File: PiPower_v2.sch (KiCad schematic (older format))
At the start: 82 parts, among them J1 MicroUSB_in, J10 5V_Pi, J11 12V_Out, J2 LiPo_JST, J3 USB_A_out, J4 Auto_On, J5 5V_USB, J6 5V_EXT, J7 5V_IN, J8 VBAT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

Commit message: 1310211033 PiPower work in progress
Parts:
- removed Q1: 2SK3019, SOT416_2SK3019, symbol 2SK3019
- removed R5: 100k, r_0805, symbol R
- removed R7: 10k, r_0805, symbol R
- R9: value 1k5 -> 4k7
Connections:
- net labels removed: EN
- wire segments 352 -> 242

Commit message: 1310271049 PiPower work in progress
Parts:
- added L?: 4u7H,1.2A, Inductor_SMD1, symbol INDUCTOR
- added R?: 100k, r_0805, symbol R
- added U2: TPS62163, symbol TPS62163
- C2: value 100u,25V -> 10u,25V, X7R
- C3: value 2u2 Tant -> 22u,25V, X7R
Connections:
- wire segments 242 -> 254
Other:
- moved on the sheet: C1, C2, C3, D1, J6
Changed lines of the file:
@@
 Text Label 7875 1050 0    40   ~ 0
 PWR_IN
-$Comp
-L GND #PWR1
-U 1 1 51E42797
-P 9700 1800
-F 0 "#PWR1" H 9700 1800 30  0001 C CNN
-F 1 "GND" H 9700 1730 30  0001 C CNN
-F 2 "" H 9700 1800 60  0001 C CNN
-F 3 "" H 9700 1800 60  0001 C CNN
-	1    9700 1800
-	-1   0    0    -1
-$EndComp
-Text Label 8900 1700 0    40   ~ 0
+Text Label 9600 1650 0    40   ~ 0
 GND
 $Comp
@@
 L DIODESCH D1
 U 1 1 51E427BE
-P 8300 1050
-F 0 "D1" H 8300 1150 40  0000 C CNN
-F 1 "LSM115J" H 8300 950 40  0000 C CNN
-F 2 "diode-DO214BA" H 8300 1050 60  0001 C CNN
-F 3 "~" H 8300 1050 60  0000 C CNN
-	1    8300 1050
-	1    0    0    -1
-$EndComp
-Text Label 9975 1050 0    40   ~ 0
+P 11700 450
+F 0 "D1" H 11700 550 40  0000 C CNN
+F 1 "LSM115J" H 11700 350 40  0000 C CNN
+F 2 "diode-DO214BA" H 11700 450 60  0001 C CNN
+F 3 "~" H 11700 450 60  0000 C CNN
+	1    11700 450
+	1    0    0    -1
+$EndComp
+Text Label 10100 1050 0    40   ~ 0
 5V_EXT
 $Comp
 L CAP_NP C1
 U 1 1 51E43023
-P 9700 1475
-F 0 "C1" H 9625 1400 40  0000 C CNN
-F 1 "100nF" H 9600 1575 40  0000 C CNN
-F 2 "c_0805" H 9700 1475 60  0001 C CNN
-F 3 "" H 9700 1475 60  0000 C CNN
-	1    9700 1475
+P 10325 1175
+F 0 "C1" H 10250 1100 40  0000 C CNN
+F 1 "100nF" V 10275 1350 40  0000 C CNN
+F 2 "c_0805" H 10325 1175 60  0001 C CNN
+F 3 "" H 10325 1175 60  0000 C CNN
+	1    10325 1175
 	-1   0    0    1
 $EndComp
@@
 L CAP_POL C2
 U 1 1 51E43043
-P 8575 1500
-F 0 "C2" H 8650 1600 40  0000 C CNN
-F 1 "100u,25V" H 8725 1425 40  0000 C CNN
-F 2 "C_ELCO_SMD" H 8575 1500 60  0001 C CNN
-F 3 "" H 8575 1500 60  0000 C CNN
-	1    8575 1500
+P 8175 1200
+F 0 "C2" H 8225 1275 40  0000 C CNN
+F 1 "10u,25V, X7R" V 8225 950 40  0000 C CNN
+F 2 "C_ELCO_SMD" H 8175 1200 60  0001 C CNN
+F 3 "" H 8175 1200 60  0000 C CNN
+	1    8175 1200
 	1    0    0    -1
 $EndComp
@@
 L CAP_POL C3
 U 1 1 51E4306C
-P 9975 1500
-F 0 "C3" H 10050 1600 40  0000 C CNN
-F 1 "2u2 Tant" H 10125 1425 40  0000 C CNN
-F 2 "c_0805" H 9975 1500 60  0001 C CNN
-F 3 "" H 9975 1500 60  0000 C CNN
-	1    9975 1500
+P 10075 1200
+F 0 "C3" H 10150 1300 40  0000 C CNN
+F 1 "22u,25V, X7R" V 10125 950 40  0000 C CNN
+F 2 "c_0805" H 10075 1200 60  0001 C CNN
+F 3 "" H 10075 1200 60  0000 C CNN
+	1    10075 1200
 	1    0    0    -1
 $EndComp
@@
 L CONN_2 J6
 U 1 1 51EBDA2C
-P 10675 1400
-F 0 "J6" V 10625 1400 40  0000 C CNN
-F 1 "5V_EXT" V 10725 1400 40  0000 C CNN
-F 2 "Header_2" H 10675 1300 60  0001 C CNN
-F 3 "~" H 10675 1300 60  0000 C CNN
-	1    10675 1400
+P 10900 1150
+F 0 "J6" V 10850 1150 40  0000 C CNN
+F 1 "5V_EXT" V 10950 1150 40  0000 C CNN
+F 2 "Header_2" H 10900 1050 60  0001 C CNN
+F 3 "~" H 10900 1050 60  0000 C CNN
+	1    10900 1150
 	1    0    0    -1
 $EndComp
@@
 L NCP1117ST50 U2
 U 1 1 52161420
-P 9150 1200
-F 0 "U2" H 8975 1575 40  0000 C CNN
-F 1 "NCP1117ST50" H 9150 1500 40  0000 C CNN
-F 2 "SOT223" H 9150 1200 60  0001 C CNN
-F 3 "~" H 9150 1200 60  0000 C CNN
-	1    9150 1200
+P 11900 1050
+F 0 "U2" H 11725 1425 40  0000 C CNN
+F 1 "NCP1117ST50" H 11900 1350 40  0000 C CNN
+F 2 "SOT223" H 11900 1050 60  0001 C CNN
+F 3 "~" H 11900 1050 60  0000 C CNN
+	1    11900 1050
 	1    0    0    -1
 $EndComp
@@
 Wire Wire Line
 	10125 2850 10125 2975
-Connection ~ 9975 1700
-Wire Wire Line
-	10275 1700 10275 1500
-Wire Wire Line
-	10275 1500 10325 1500
-Connection ~ 9975 1050
-Wire Wire Line
-	10275 1050 10275 1300
-Wire Wire Line
-	10275 1300 10325 1300
 Connection ~ 5400 3375
 Wire Wire Line
@@
 	5550 2125 5550 1900
 Wire Wire Line
-	9550 1050 10275 1050
-Wire Wire Line
-	8575 1050 8575 1400
-Connection ~ 8575 1050
-Wire Wire Line
-	9700 1575 9700 1800
-Wire Wire Line
 	7850 1250 7925 1250
 Wire Wire Line
 	7925 1150 7850 1150
-Connection ~ 9700 1700
-Wire Wire Line
-	9975 1700 9975 1575
-Wire Wire Line
-	9975 1050 9975 1400
-Wire Wire Line
-	8575 1700 10275 1700
-Wire Wire Line
-	8575 1575 8575 1700
-Wire Wire Line
-	7850 1050 8100 1050
+Wire Wire Line
+	7850 1050 8450 1050
 Wire Wire Line
 	7925 1150 7925 1800
-Wire Wire Line
-	9150 1800 9150 1600
-Connection ~ 9150 1700
-Connection ~ 9700 1050
-Wire Wire Line
-	8500 1050 8750 1050
-Wire Wire Line
-	9700 1050 9700 1400
 Wire Wire Line
 	5200 7175 5200 6400
@@
 Wire Wire Line
 	8025 1050 8025 1700
-Connection ~ 8025 1050
 Wire Wire Line
 	7800 1600 7925 1600
 Connection ~ 7925 1600
 Wire Wire Line
-	7800 1800 9150 1800
-Wire Wire Line
 	8025 1700 7800 1700
 Connection ~ 8025 1500
-Connection ~ 7925 1800
 Wire Wire Line
 	1225 1500 1300 1500
@@
 	3250 3375 3100 3375
 Connection ~ 3100 3375
+$Comp
+L TPS62163 U2
+U 1 1 526D1432
+P 8800 1400
+F 0 "U2" H 8550 1850 40  0000 L BNN
+F 1 "TPS62163" H 8550 1050 40  0000 L TNN
+F 2 "" H 8800 1700 60  0000 C CNN
+F 3 "" H 8800 1700 60  0000 C CNN
+	1    8800 1400
+	1    0    0    -1
+$EndComp
+$Comp
+L INDUCTOR L?
+U 1 1 526D14F0
+P 9550 1050
+F 0 "L?" V 9500 1050 40  0000 C CNN
+F 1 "4u7H,1.2A" V 9650 1050 40  0000 C CNN
+F 2 "Inductor_SMD1" H 9550 1050 60  0001 C CNN
+F 3 "~" H 9550 1050 60  0000 C CNN
+	1    9550 1050
+	0    -1   -1   0
+$EndComp
+$Comp
+L R R?
+U 1 1 526D1586
+P 9500 1250
+F 0 "R?" V 9550 1450 40  0000 C CNN
+F 1 "100k" V 9500 1250 40  0000 C CNN
+F 2 "r_0805" H 9500 1250 60  0001 C CNN
+F 3 "" H 9500 1250 60  0000 C CNN
+	1    9500 1250
+	0    -1   -1   0
+$EndComp
+$Comp
+L GND #PWR1
+U 1 1 51E42797
+P 8375 1925
+F 0 "#PWR1" H 8375 1925 30  0001 C CNN
+F 1 "GND" H 8375 1855 30  0001 C CNN
+F 2 "" H 8375 1925 60  0001 C CNN
+F 3 "" H 8375 1925 60  0001 C CNN
+	1    8375 1925
+	-1   0    0    -1
+$EndComp
+Wire Wire Line
+	9150 1150 9925 1150
+Wire Wire Line
+	9925 1050 9925 1250
+Wire Wire Line
+	9850 1050 10550 1050
+Wire Wire Line
+	9250 1050 9150 1050
+Wire Wire Line
+	10075 1050 10075 1100
+Wire Wire Line
+	10325 1050 10325 1100
+Wire Wire Line
+	9150 1250 9250 1250
+Wire Wire Line
+	9925 1250 9750 1250
+Connection ~ 9925 1150
+Connection ~ 10075 1050
+Connection ~ 9925 1050
+Wire Wire Line
+	10325 1275 10325 1650
+Wire Wire Line
+	9150 1650 10475 1650
+Wire Wire Line
+	9150 1350 9250 1350
+Wire Wire Line
+	9250 1350 9250 1800
+Connection ~ 9250 1650
+Wire Wire Line
+	9150 1550 9250 1550
+Connection ~ 9250 1550
+Wire Wire Line
+	8175 1050 8175 1100
+Wire Wire Line
+	8450 1150 8375 1150
+Wire Wire Line
+	8375 1150 8375 1050
+Connection ~ 8375 1050
+Wire Wire Line
+	8450 1250 8375 1250
+Wire Wire Line
+	8175 1650 8450 1650
+Wire Wire Line
+	8375 1250 8375 1925
+Wire Wire Line
+	8450 1350 8375 1350
+Connection ~ 8375 1350
+Wire Wire Line
+	8450 1450 8375 1450
+Connection ~ 8375 1450
+Wire Wire Line
+	8450 1550 8375 1550
+Connection ~ 8375 1550
+Wire Wire Line
+	8175 1275 8175 1650
+Connection ~ 8375 1650
+Connection ~ 10325 1050
+Wire Wire Line
+	10550 1250 10475 1250
+Wire Wire Line
+	10475 1250 10475 1650
+Connection ~ 10325 1650
+Wire Wire Line
+	10075 1275 10075 1650
+Connection ~ 10075 1650
+Connection ~ 8175 1050
+Connection ~ 8025 1050
+Connection ~ 7925 1800
+Wire Wire Line
+	9250 1800 7800 1800
+Connection ~ 8375 1800
 $EndSCHEMATC

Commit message: 1311021119 Schematic complete, needs to be verified
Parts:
- removed D1, D5: LSM115J, diode-DO214BA, symbol DIODESCH
- removed SJ5: STAT, ShortLink, symbol LINK1
- removed U2: NCP1117ST50, SOT223, symbol NCP1117ST50
- added J12: 5V_IN, symbol CONN_3
- added SJ5: STAT, symbol LINK2
- D7: value EXT_ON -> 5V_OUT
- J7: value 5V_IN -> 5V_OUT
- SJ2: value Ext_On -> 5V_OUT
- gave numbers to parts that had none: 2
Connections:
- net labels added: 5V_OUT
- wire segments 254 -> 256
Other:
- note added: "12V INPUT (5V-12V)"
- note added: "5V USB INPUT"
- note added: "Auto-Switch (5V_IN <> 5V_BAT)"
- note added: "Boost Converter (3.7V to 5V Bat)"
- note added: "LiPo Charger (3.7V)"
- note added: "LiPo Fuel Gauge I2C"
- note added: "Manual Selector"
- note added: "Power Switch"
- note added: "Ras-Pi GPIO Header"
- note removed: "3.7V to 5V Boost Conv.\nVBAT is LiPo 3.7V\n5V_BAT is output from Boost conv\n\nEN input of U4 controls auto-switching.\nWhen 5V_IN is On, EN is LOW, U4 is SHUT\nWhen 5V_IN is Off, EN is HI, U4 OPERATES"
- note removed: "5V INPUT at J2, Micro USB\nU1 charges 3.7V LiPo\nLiPo connects to J3\n\nEDIT :\nR3 changed from \n1k5 (500mA) to 4k7 (200mA)\n\nR1/R2 changed from\n1k5 to 4k7\n\nAdded Shorting Link for LEDs"
- note removed: "Auto Switch selector\nExt 12V <> uUSB 5V\n\nAdded Jumper link\nto disable LED"
- note removed: "Ext 7V to 12V Barrel Socket"
- note removed: "Li-Po Battery\nFuel Gauge"
- note removed: "Power Switcher.\n5V_Pi to Ras-Pi\nGPIO4 monitored on Ras-Pi\nSW1 to switch On/Off Ras-Pi\nJumper J1 allows Auto On. \n ON = Ras-Pi On when power applied\n OFF = Ras-Pi to be turned On by SW1\nR21 prevents Ras-Pi GPIO4 damage due to 5V\n\nNormal operation : 5V_IN from uUSB powers Ras-Pi\nLiPo is charged via U1\n5V_BAT cannot operate Ras-Pi due to D5 reverse bias\nWhen 5V_IN is cut off, 5V_BAT powe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"
- note removed: "Swapped Off and On on J4\nAdded LED for 5V_Pi indication\nAdded 470k (R23)"
- moved on the sheet: C1, C10, C11, C12, C13, C14, C15, C16, C17, C18, C2, C3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

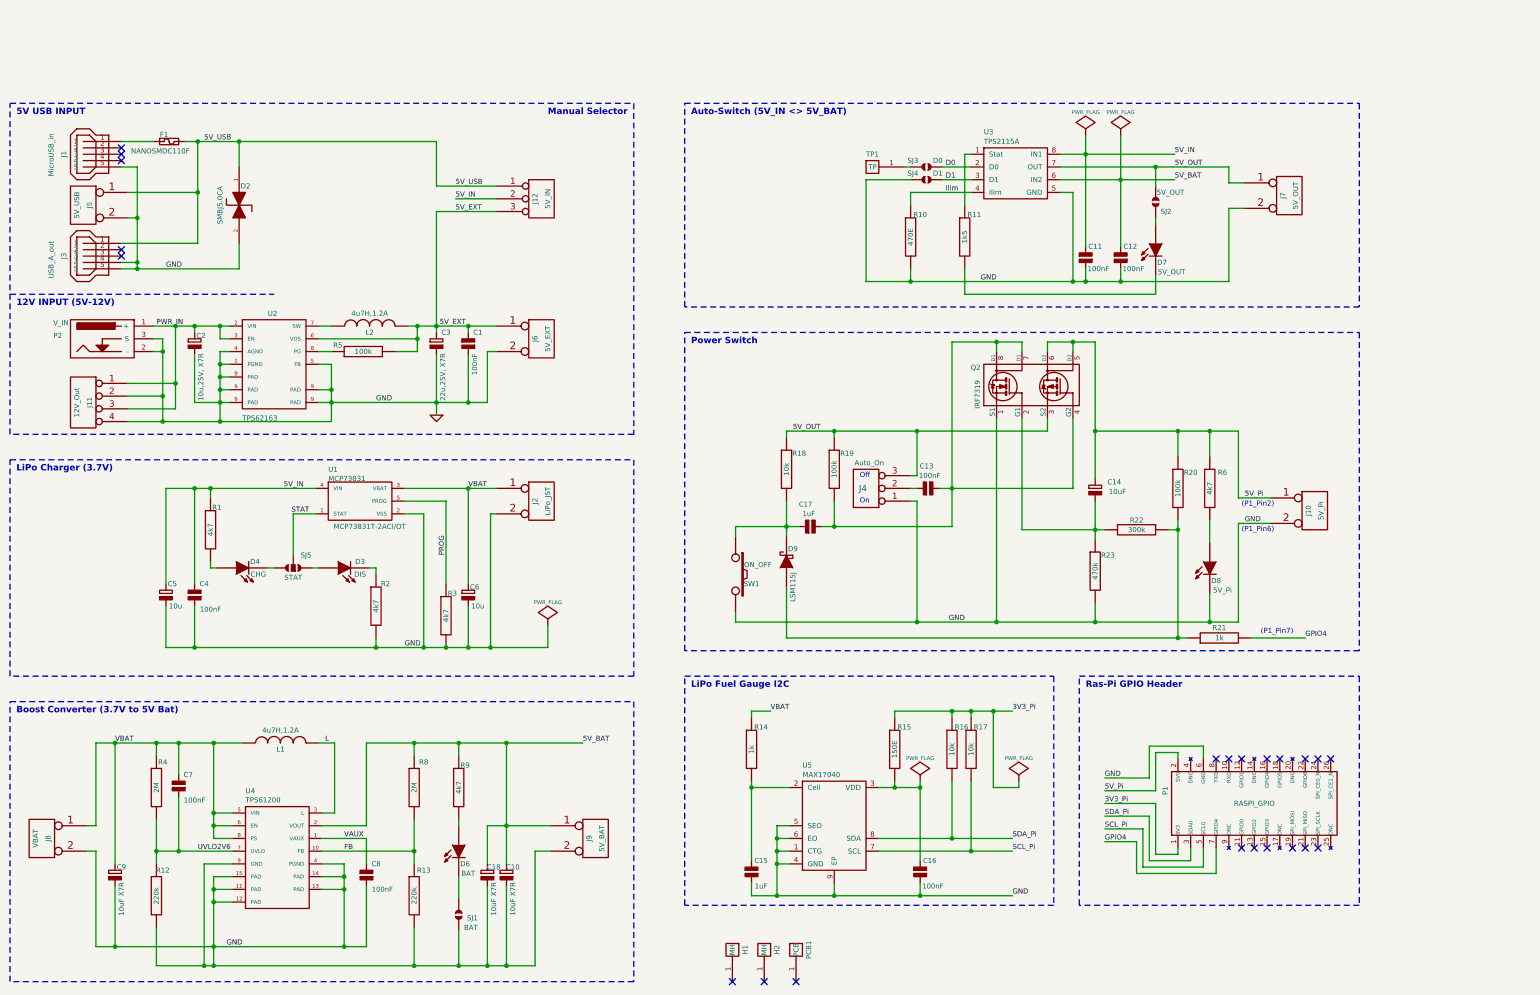
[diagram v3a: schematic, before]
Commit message: 1311031620 Schematic complete, needs to be verified
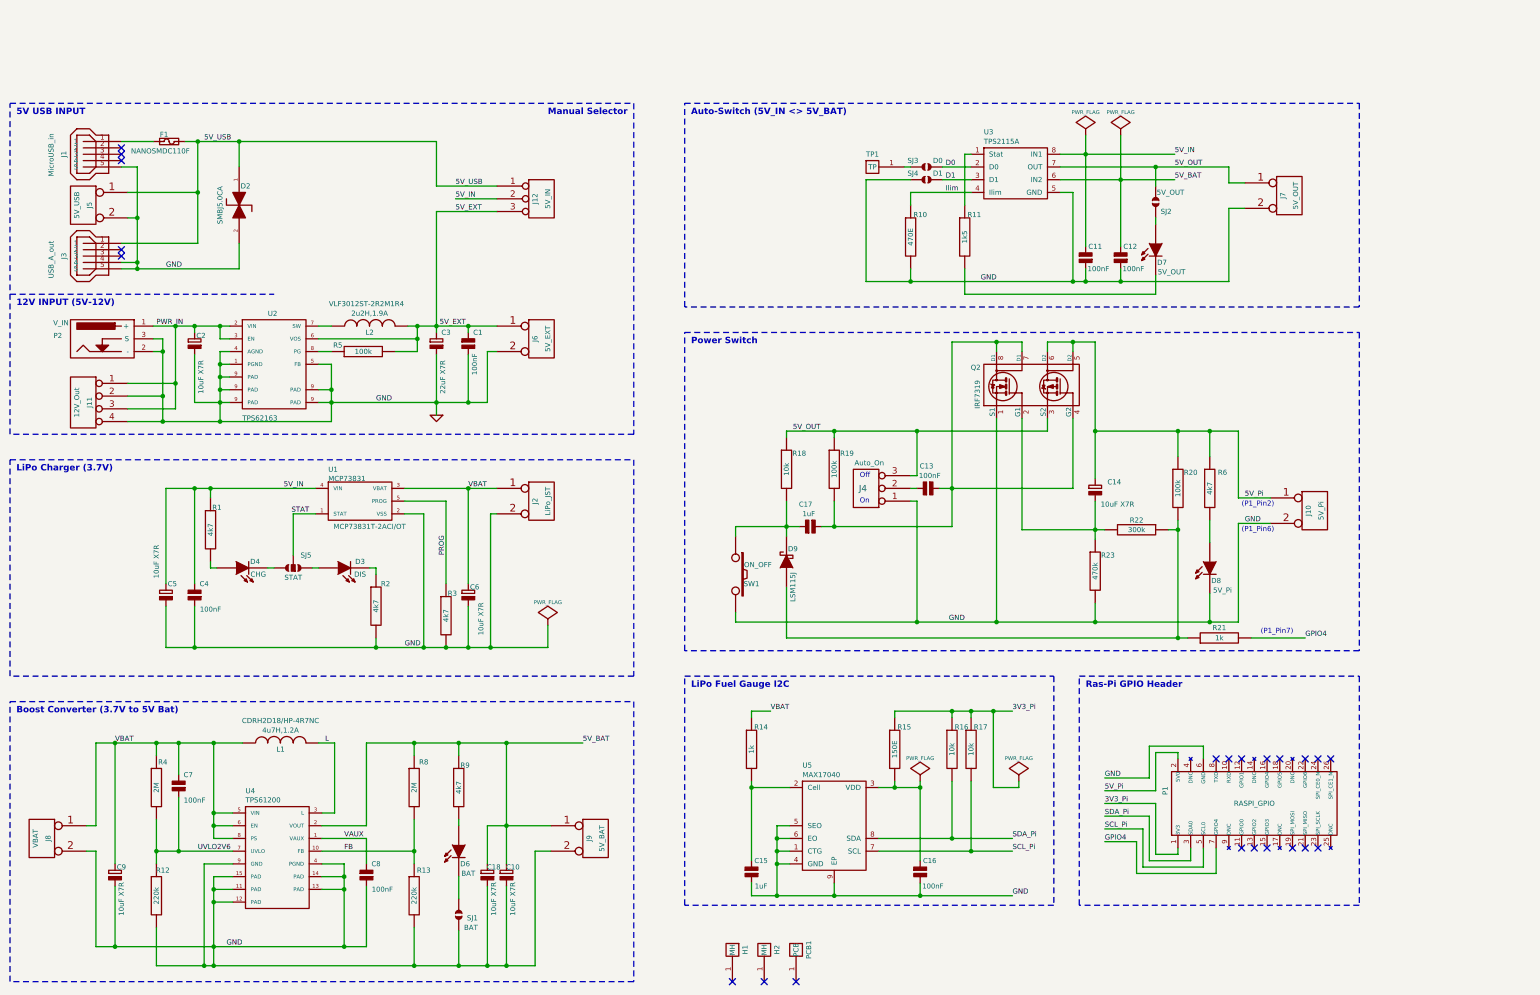
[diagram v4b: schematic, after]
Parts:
- C14: value 10uF -> 10uF X7R
- C2: value 10u,25V, X7R -> 10uF X7R
- C3: value 22u,25V, X7R -> 22uF X7R
- C5, C6: value 10u -> 10uF X7R
- L1: Mfr_PN (none) -> CDRH2D18/HP-4R7NC
- L2: value 4u7H,1.2A -> 2u2H,1.9A; Mfr_PN (none) -> VLF3012ST-2R2M1R4
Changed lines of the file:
@@
 P 9075 3700
 F 0 "C14" H 9225 3775 40  0000 C CNN
-F 1 "10uF" H 9250 3700 40  0000 C CNN
+F 1 "10uF X7R" H 9250 3600 40  0000 C CNN
 F 2 "C_ELCO_SMD" H 9075 3700 60  0001 C CNN
 F 3 "" H 9075 3700 60  0000 C CNN
@@
 P 1775 4525
 F 0 "C5" H 1825 4625 40  0000 C CNN
-F 1 "10u" H 1850 4450 40  0000 C CNN
+F 1 "10uF X7R" V 1700 4800 40  0000 C CNN
 F 2 "C_ELCO_SMD" H 1775 4525 60  0001 C CNN
 F 3 "" H 1775 4525 60  0000 C CNN
@@
 P 4150 4525
 F 0 "C6" H 4200 4600 40  0000 C CNN
-F 1 "10u" H 4225 4450 39  0000 C CNN
+F 1 "10uF X7R" V 4250 4350 39  0000 C CNN
 F 2 "C_ELCO_SMD" H 4150 4525 60  0001 C CNN
 F 3 "" H 4150 4525 60  0000 C CNN
@@
 F 2 "Inductor_SMD1" H 2675 5675 60  0001 C CNN
 F 3 "~" H 2675 5675 60  0000 C CNN
+F 4 "CDRH2D18/HP-4R7NC" V 2850 5675 40  0000 C CNN "Mfr_PN"
 	1    2675 5675
 	0    -1   -1   0
@@
 P 2000 2550
 F 0 "C2" H 2050 2625 40  0000 C CNN
-F 1 "10u,25V, X7R" V 2050 2300 40  0000 C CNN
+F 1 "10uF X7R" V 2050 2300 40  0000 C CNN
 F 2 "C_ELCO_SMD" H 2000 2550 60  0001 C CNN
 F 3 "" H 2000 2550 60  0000 C CNN
@@
 P 3900 2550
 F 0 "C3" H 3975 2650 40  0000 C CNN
-F 1 "22u,25V, X7R" V 3950 2300 40  0000 C CNN
+F 1 "22uF X7R" V 3950 2300 40  0000 C CNN
 F 2 "c_0805" H 3900 2550 60  0001 C CNN
 F 3 "" H 3900 2550 60  0000 C CNN
@@
 P 3375 2400
 F 0 "L2" V 3325 2400 40  0000 C CNN
-F 1 "4u7H,1.2A" V 3475 2400 40  0000 C CNN
+F 1 "2u2H,1.9A" V 3475 2400 40  0000 C CNN
 F 2 "Inductor_SMD1" H 3375 2400 60  0001 C CNN
 F 3 "~" H 3375 2400 60  0000 C CNN
+F 4 "VLF3012ST-2R2M1R4" V 3550 2425 40  0000 C CNN "Mfr_PN"
 	1    3375 2400
 	0    -1   -1   0

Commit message: 1311060933 changed some resistor values for charging current and LEDs
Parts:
- added SJ6: 5V_Pi, ShortLink, symbol LINK1
- R1, R2, R6, R9: value 4k7 -> 2k2
- R3: value 4k7 -> 2k
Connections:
- net GND: now also SJ6.2; no longer D8.2 (K)
- new net: D8.2 (K), SJ6.1
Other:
- note added: "R3 :\n2k0 for 500mA\n4k7 for 200mA"
- moved on the sheet: C14, D8, R20, R22, R6
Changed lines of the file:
@@
 L CAP_POL C14
 U 1 1 51D06C0F
-P 9075 3700
-F 0 "C14" H 9225 3775 40  0000 C CNN
-F 1 "10uF X7R" H 9250 3600 40  0000 C CNN
-F 2 "C_ELCO_SMD" H 9075 3700 60  0001 C CNN
-F 3 "" H 9075 3700 60  0000 C CNN
-	1    9075 3700
+P 9075 3400
+F 0 "C14" H 9225 3475 40  0000 C CNN
+F 1 "10uF X7R" H 9250 3300 40  0000 C CNN
+F 2 "C_ELCO_SMD" H 9075 3400 60  0001 C CNN
+F 3 "" H 9075 3400 60  0000 C CNN
+	1    9075 3400
 	1    0    0    -1
 $EndComp
@@
 L R R20
 U 1 1 51D06C2C
-P 9725 3675
-F 0 "R20" H 9825 3800 40  0000 C CNN
-F 1 "100k" V 9725 3675 40  0000 C CNN
-F 2 "r_0805" H 9725 3675 60  0001 C CNN
-F 3 "" H 9725 3675 60  0000 C CNN
-	1    9725 3675
+P 9725 3525
+F 0 "R20" H 9825 3650 40  0000 C CNN
+F 1 "100k" V 9725 3525 40  0000 C CNN
+F 2 "r_0805" H 9725 3525 60  0001 C CNN
+F 3 "" H 9725 3525 60  0000 C CNN
+	1    9725 3525
 	1    0    0    -1
 $EndComp
@@
 L R R22
 U 1 1 51D06C32
-P 9400 4000
-F 0 "R22" V 9325 4000 40  0000 C CNN
-F 1 "300k" V 9400 4000 40  0000 C CNN
-F 2 "r_0805" H 9400 4000 60  0001 C CNN
-F 3 "" H 9400 4000 60  0000 C CNN
-	1    9400 4000
+P 9400 3850
+F 0 "R22" V 9325 3850 40  0000 C CNN
+F 1 "300k" V 9400 3850 40  0000 C CNN
+F 2 "r_0805" H 9400 3850 60  0001 C CNN
+F 3 "" H 9400 3850 60  0000 C CNN
+	1    9400 3850
 	0    1    1    0
 $EndComp
@@
 P 2125 4000
 F 0 "R1" H 2175 4175 40  0000 C CNN
-F 1 "4k7" V 2125 4000 40  0000 C CNN
+F 1 "2k2" V 2125 4000 40  0000 C CNN
 F 2 "r_0805" H 2125 4000 60  0001 C CNN
 F 3 "" H 2125 4000 60  0000 C CNN
@@
 P 3975 4675
 F 0 "R3" H 4025 4850 40  0000 C CNN
-F 1 "4k7" V 3975 4675 40  0000 C CNN
+F 1 "2k" V 3975 4675 40  0000 C CNN
 F 2 "r_0805" H 3975 4675 60  0001 C CNN
 F 3 "" H 3975 4675 60  0000 C CNN
@@
 P 3425 4600
 F 0 "R2" H 3500 4775 40  0000 C CNN
-F 1 "4k7" V 3425 4600 40  0000 C CNN
+F 1 "2k2" V 3425 4600 40  0000 C CNN
 F 2 "r_0805" H 3425 4600 60  0001 C CNN
 F 3 "" H 3425 4600 60  0000 C CNN
@@
 P 4075 6025
 F 0 "R9" H 4125 6200 40  0000 C CNN
-F 1 "4k7" V 4075 6025 40  0000 C CNN
+F 1 "2k2" V 4075 6025 40  0000 C CNN
 F 2 "r_0805" H 4075 6025 60  0001 C CNN
 F 3 "" H 4075 6025 60  0000 C CNN
@@
 L R R6
 U 1 1 524D93B8
-P 9975 3675
-F 0 "R6" H 10075 3800 40  0000 C CNN
-F 1 "4k7" V 9975 3675 40  0000 C CNN
-F 2 "r_0805" H 9975 3675 60  0001 C CNN
-F 3 "" H 9975 3675 60  0000 C CNN
-	1    9975 3675
+P 9975 3525
+F 0 "R6" H 10075 3650 40  0000 C CNN
+F 1 "2k2" V 9975 3525 40  0000 C CNN
+F 2 "r_0805" H 9975 3525 60  0001 C CNN
+F 3 "" H 9975 3525 60  0000 C CNN
+	1    9975 3525
 	1    0    0    -1
 $EndComp
@@
 L LED D8
 U 1 1 524D93BE
-P 9975 4300
-F 0 "D8" V 10075 4350 40  0000 C CNN
-F 1 "5V_Pi" V 10150 4400 40  0000 C CNN
-F 2 "led_0805" H 9975 4300 60  0001 C CNN
-F 3 "~" H 9975 4300 60  0000 C CNN
-	1    9975 4300
+P 9975 4050
+F 0 "D8" V 10075 4100 40  0000 C CNN
+F 1 "5V_Pi" V 10150 4150 40  0000 C CNN
+F 2 "led_0805" H 9975 4050 60  0001 C CNN
+F 3 "~" H 9975 4050 60  0000 C CNN
+	1    9975 4050
 	0    1    1    0
 $EndComp
@@
 	1425 1150 1550 1150
 Wire Wire Line
-	8500 3125 8500 4000
+	8500 3125 8500 3850
 Wire Wire Line
 	7950 3975 6925 3975
@@
 	10300 4850 10725 4850
 Wire Wire Line
-	9075 3775 9075 4075
-Wire Wire Line
-	8500 4000 9150 4000
-Wire Wire Line
-	9725 3925 9725 4850
-Wire Wire Line
-	9725 3225 9725 3425
+	9075 3475 9075 4075
+Wire Wire Line
+	8500 3850 9150 3850
+Wire Wire Line
+	9725 3775 9725 4850
+Wire Wire Line
+	9725 3225 9725 3275
 Wire Wire Line
 	9075 3225 10200 3225
 Wire Wire Line
-	9075 2525 9075 3600
+	9075 2525 9075 3300
 Connection ~ 6650 3975
 Connection ~ 7025 3975
@@
 	6250 4725 6250 4650
 Connection ~ 7675 4725
-Connection ~ 9075 4000
-Wire Wire Line
-	9650 4000 9725 4000
-Connection ~ 9725 4000
+Connection ~ 9075 3850
+Wire Wire Line
+	9650 3850 9725 3850
+Connection ~ 9725 3850
 Connection ~ 9725 4850
 Wire Wire Line
-	9975 3925 9975 4100
-Wire Wire Line
-	9975 4500 9975 4725
-Connection ~ 9975 4725
-Wire Wire Line
-	9975 3425 9975 3225
+	9975 3775 9975 3850
+Wire Wire Line
+	9975 3275 9975 3225
 Connection ~ 9975 3225
 Wire Wire Line
@@
 Text Notes 9000 5250 0    50   ~ 10
 Ras-Pi GPIO Header
+Text Notes 4700 4250 0    40   ~ 0
+R3 :\n2k0 for 500mA\n4k7 for 200mA
+$Comp
+L LINK1 SJ6
+U 1 1 527A5922
+P 9975 4475
+F 0 "SJ6" V 10050 4600 40  0000 R CNN
+F 1 "5V_Pi" V 9925 4650 40  0000 R CNN
+F 2 "ShortLink" H 9975 4475 60  0001 C CNN
+F 3 "" H 9975 4475 60  0000 C CNN
+	1    9975 4475
+	0    1    1    0
+$EndComp
+Wire Wire Line
+	9975 4250 9975 4350
+Wire Wire Line
+	9975 4600 9975 4725
+Connection ~ 9975 4725
 $EndSCHEMATC
